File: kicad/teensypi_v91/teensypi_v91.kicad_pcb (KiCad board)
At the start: 2 copper layers, 94 x 91.9 mm, 36 parts, among them M1_center1 MountingHole, M2_center1 MountingHole, M3_center1 MountingHole, M4_center1 MountingHole

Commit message: modified:   kicad/teensypi_v91/teensypi_v91.kicad_pcb
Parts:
- added GND_PAD10: Conn_01x01, Connector_Wire:SolderWirePad_1x01_SMD_5x10mm, F.Cu at (151.0, 65.0)
- added GND_PAD11: Conn_01x01, Connector_Wire:SolderWirePad_1x01_SMD_5x10mm, F.Cu at (151.0, 69.0)
- added GND_PAD12: Conn_01x01, Connector_Wire:SolderWirePad_1x01_SMD_5x10mm, F.Cu at (151.0, 72.0)
- added GND_PAD13: Conn_01x01, Connector_Wire:SolderWirePad_1x01_SMD_5x10mm, F.Cu at (151.0, 76.0)
- added GND_PAD14: Conn_01x01, Connector_Wire:SolderWirePad_1x01_SMD_5x10mm, F.Cu at (160.0, 67.0)
- added GND_PAD15: Conn_01x01, Connector_Wire:SolderWirePad_1x01_SMD_5x10mm, F.Cu at (160.0, 71.0)
- added GND_PAD16: Conn_01x01, Connector_Wire:SolderWirePad_1x01_SMD_5x10mm, F.Cu at (160.0, 74.0)
- added GND_PAD17: Conn_01x01, Connector_Wire:SolderWirePad_1x01_SMD_5x10mm, F.Cu at (160.0, 77.0)
- added GND_PAD2: Conn_01x01, Connector_Wire:SolderWirePad_1x01_SMD_5x10mm, F.Cu at (145.0, 62.0)
- added GND_PAD3: Conn_01x01, Connector_Wire:SolderWirePad_1x01_SMD_5x10mm, F.Cu at (145.0, 66.0)
- added GND_PAD4: Conn_01x01, Connector_Wire:SolderWirePad_1x01_SMD_5x10mm, F.Cu at (145.0, 70.0)
- added GND_PAD5: Conn_01x01, Connector_Wire:SolderWirePad_1x01_SMD_5x10mm, F.Cu at (145.0, 74.0)
- added GND_PAD6: Conn_01x01, Connector_Wire:SolderWirePad_1x01_SMD_5x10mm, F.Cu at (166.0, 64.0)
- added GND_PAD7: Conn_01x01, Connector_Wire:SolderWirePad_1x01_SMD_5x10mm, F.Cu at (166.0, 67.0)
- added GND_PAD8: Conn_01x01, Connector_Wire:SolderWirePad_1x01_SMD_5x10mm, F.Cu at (166.0, 71.0)
- added GND_PAD9: Conn_01x01, Connector_Wire:SolderWirePad_1x01_SMD_5x10mm, F.Cu at (166.0, 74.0)

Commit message: Removed PCB courtyards
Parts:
- turned GND_PAD2 to 180 degrees

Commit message: modified:   kicad/teensypi_v91/teensypi_v91.kicad_pcb
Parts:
- added GND_PAD18: Conn_01x01, Connector_Wire:SolderWirePad_1x01_SMD_5x10mm, F.Cu at (164.1, 112.5)
- added GND_PAD19: Conn_01x01, Connector_Wire:SolderWirePad_1x01_SMD_5x10mm, F.Cu at (164.1, 107.9)
- added GND_PAD20: Conn_01x01, Connector_Wire:SolderWirePad_1x01_SMD_5x10mm, F.Cu at (164.1, 115.4)
- added GND_PAD21: Conn_01x01, Connector_Wire:SolderWirePad_1x01_SMD_5x10mm, F.Cu at (164.1, 118.5)
- moved GND_PAD14 12.9 mm to (161.9, 79.8)
- moved GND_PAD15 12.9 mm to (161.9, 83.8)
- moved GND_PAD7 7.75 mm to (166.5, 74.7)
- moved GND_PAD6 7.59 mm to (166.6, 71.6)
- moved GND_PAD8 5.98 mm to (166.9, 76.9)
- moved GND_PAD9 5.31 mm to (166.7, 79.3)
- moved GND_PAD16 4.57 mm to (161.9, 78.1)
- moved GND_PAD17 4.49 mm to (162.1, 81.0)
- moved REG1 3.98 mm to (148.0, 106.0)
- moved Motor4 3.13 mm to (137.7, 78.7)
- moved Motor1 2.94 mm to (170.3, 74.8)
- moved M_1_3 2.87 mm to (190.0, 54.1)
- moved Motor2 2.25 mm to (173.8, 108.3)
- moved GND_PAD10 1.78 mm to (152.8, 64.8)
- moved GND_PAD11 1.78 mm to (152.8, 68.8)
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
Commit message: modified:   kicad/teensypi_v91/teensypi_v91.kicad_pcb
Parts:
- moved M_3_4 10.0 mm to (121.5, 132.2)
- moved M_2_4 4.76 mm to (191.8, 131.2)
- moved M_3_2 4.56 mm to (116.5, 127.2)
- moved M_3_3 3.88 mm to (116.2, 137.0)
- moved M_4_4 3.75 mm to (117.0, 60.2)
- moved M_4_1 3.24 mm to (116.8, 50.2)
- moved M_4_3 3.15 mm to (122.2, 54.2)
- moved M_4_2 2.94 mm to (112.5, 55.5)
- moved M_3_1 2.86 mm to (111.0, 132.2)
- moved M_2_3 2.80 mm to (196.5, 137.2)
- moved M_2_1 2.30 mm to (196.2, 127.5)
- moved M2_center1 1.06 mm to (196.8, 132.8)
- moved M_2_2 1.06 mm to (201.8, 131.4)
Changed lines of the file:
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@@
 	(footprint "MountingHole:MountingHole_2.2mm_M2"
 		(layer "F.Cu")
-		(at 120 136)
+		(at 116.25 137)
 		(descr "Mounting Hole 2.2mm, no annular, M2")
 		(tags "mounting hole 2.2mm no annular m2")
@@
 	(footprint "MountingHole:MountingHole_2.2mm_M2"
 		(layer "F.Cu")
-		(at 111.801001 135)
+		(at 111 132.25)
 		(descr "Mounting Hole 2.2mm, no annular, M2")
 		(tags "mounting hole 2.2mm no annular m2")
@@
 	(footprint "MountingHole:MountingHole_2.2mm_M2"
 		(layer "F.Cu")
-		(at 192 136)
+		(at 191.75 131.25)
 		(descr "Mounting Hole 2.2mm, no annular, M2")
 		(tags "mounting hole 2.2mm no annular m2")
@@
 		)
 		(pad "" np_thru_hole circle
-			(at 0 0)
+			(at -1 0)
 			(size 2.2 2.2)
 			(drill 2.2)
@@
 	(footprint "MountingHole:MountingHole_2.2mm_M2"
 		(layer "F.Cu")
-		(at 199 136)
+		(at 196.5 137.25)
 		(descr "Mounting Hole 2.2mm, no annular, M2")
 		(tags "mounting hole 2.2mm no annular m2")
@@
 		)
 		(pad "" np_thru_hole circle
-			(at 0 0)
+			(at -0.75 -0.5)
 			(size 2.2 2.2)
 			(drill 2.2)
@@
 	(footprint "MountingHole:MountingHole_2.2mm_M2"
 		(layer "F.Cu")
-		(at 112 129)
+		(at 121.5 132.158893)
 		(descr "Mounting Hole 2.2mm, no annular, M2")
 		(tags "mounting hole 2.2mm no annular m2")
@@
 	(footprint "MountingHole:MountingHole_2.2mm_M2"
 		(layer "F.Cu")
-		(at 120 58)
+		(at 117 60.25)
 		(descr "Mounting Hole 2.2mm, no annular, M2")
 		(tags "mounting hole 2.2mm no annular m2")
@@
 		)
 		(pad "" np_thru_hole circle
-			(at 0 0)
+			(at 0.3 -0.25)
 			(size 2.2 2.2)
 			(drill 2.2)
@@
 	(footprint "MountingHole:MountingHole_2.2mm_M2"
 		(layer "F.Cu")
-		(at 114.05 52.05)
+		(at 116.75 50.25)
 		(descr "Mounting Hole 2.2mm, no annular, M2")
 		(tags "mounting hole 2.2mm no annular m2")
@@
 	(footprint "MountingHole:MountingHole_2.2mm_M2"
 		(layer "F.Cu")
-		(at 201 130.65)
+		(at 201.75 131.4)
 		(descr "Mounting Hole 2.2mm, no annular, M2")
 		(tags "mounting hole 2.2mm no annular m2")
@@
 		)
 		(pad "" np_thru_hole circle
-			(at 0 0)
+			(at -0.75 0.35)
 			(size 2.2 2.2)
 			(drill 2.2)
@@
 	(footprint "MountingHole:MountingHole_2.2mm_M2"
 		(layer "F.Cu")
-		(at 194 127)
+		(at 196.25 127.5)
 		(descr "Mounting Hole 2.2mm, no annular, M2")
 		(tags "mounting hole 2.2mm no annular m2")
@@
 		)
 		(pad "" np_thru_hole circle
-			(at 0 0)
+			(at -0.5 -0.5)
 			(size 2.2 2.2)
 			(drill 2.2)
@@
 	(footprint "MountingHole:MountingHole_5.5mm"
 		(layer "F.Cu")
-		(at 196 132)
+		(at 196.75 132.75)
 		(descr "Mounting Hole 5.5mm, no annular")
 		(tags "mounting hole 5.5mm no annular")
@@
 		)
 		(pad "" np_thru_hole circle
-			(at 0 0)
+			(at -0.75 -0.75)
 			(size 5.5 5.5)
 			(drill 5.5)
@@
 	(footprint "MountingHole:MountingHole_2.2mm_M2"
 		(layer "F.Cu")
-		(at 120 52.05)
+		(at 122.25 54.25)
 		(descr "Mounting Hole 2.2mm, no annular, M2")
 		(tags "mounting hole 2.2mm no annular m2")
@@
 		)
 		(pad "" np_thru_hole circle
-			(at 0 0)
+			(at -0.25 0.75)
 			(size 2.2 2.2)
 			(drill 2.2)
@@
 	(footprint "MountingHole:MountingHole_2.2mm_M2"
 		(layer "F.Cu")
-		(at 114.05 58)
+		(at 112.5 55.5)
 		(descr "Mounting Hole 2.2mm, no annular, M2")
 		(tags "mounting hole 2.2mm no annular m2")
@@
 		)
 		(pad "" np_thru_hole circle
-			(at 0 0)
+			(at -0.3 -0.2)
 			(size 2.2 2.2)
 			(drill 2.2)
@@
 	(footprint "MountingHole:MountingHole_2.2mm_M2"
 		(layer "F.Cu")
-		(at 121 128)
+		(at 116.5 127.25)
 		(descr "Mounting Hole 2.2mm, no annular, M2")
 		(tags "mounting hole 2.2mm no annular m2")

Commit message: modified:   teensypi_v91/teensypi_v91.kicad_pcb
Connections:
- GND_PAD10 pad 1: unconnected-(GND_PAD10-Pin_1-Pad1) -> /3V3
- GND_PAD11 pad 1: unconnected-(GND_PAD11-Pin_1-Pad1) -> /GND
- GND_PAD13 pad 1: unconnected-(GND_PAD13-Pin_1-Pad1) -> /INT
- GND_PAD14 pad 1: unconnected-(GND_PAD14-Pin_1-Pad1) -> /SCL0
- GND_PAD15 pad 1: unconnected-(GND_PAD15-Pin_1-Pad1) -> /SDA0
- GND_PAD16 pad 1: unconnected-(GND_PAD16-Pin_1-Pad1) -> /3V3
- GND_PAD18 pad 1: unconnected-(GND_PAD18-Pin_1-Pad1) -> /GND
- GND_PAD19 pad 1: unconnected-(GND_PAD19-Pin_1-Pad1) -> /5V
- GND_PAD2 pad 1: /3V3 -> unconnected-(GND_PAD2-Pin_1-Pad1)
- GND_PAD20 pad 1: unconnected-(GND_PAD20-Pin_1-Pad1) -> /RX5
- GND_PAD21 pad 1: unconnected-(GND_PAD21-Pin_1-Pad1) -> /TX5
- GND_PAD3 pad 1: /GND -> unconnected-(GND_PAD3-Pin_1-Pad1)
- Motor1 pad 1: unconnected-(Motor1-Pin_1-Pad1) -> /VBAT
- Motor2 pad 1: unconnected-(Motor2-Pin_1-Pad1) -> /VBAT
- Motor3 pad 1: unconnected-(Motor3-Pin_1-Pad1) -> /VBAT
- Motor3 pad 2: /M4 -> /M3
- Motor4 pad 1: unconnected-(Motor4-Pin_1-Pad1) -> /VBAT
- Motor4 pad 2: /M3 -> /M4
- Teensy_bottom1 pad 12: unconnected-(Teensy_bottom1-Pin_12-Pad12) -> /LED_MCU
- Teensy_bottom1 pad 13: unconnected-(Teensy_bottom1-Pin_13-Pad13) -> /M3
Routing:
- net /GND: track 2.34 -> 151.4 mm
- net /3V3: track 0.00 -> 82.8 mm, vias 0 -> 1
- net /VBAT: track 0.00 -> 62.5 mm
- net /SCK: track 0.00 -> 44.1 mm, vias 0 -> 2
- net /SCL0: track 0.00 -> 37.5 mm, vias 0 -> 2
- net /5V: track 0.00 -> 32.6 mm, vias 0 -> 1
- net /MISO: track 0.00 -> 21.1 mm
- net /CS: track 0.00 -> 20.0 mm
- net /TX5: track 0.00 -> 19.9 mm, vias 0 -> 2
- net /MOSI: track 0.00 -> 18.2 mm
- net /RX5: track 0.00 -> 14.8 mm
- net /LED_MCU: track 0.00 -> 14.3 mm, vias 0 -> 2
- net /M1: track 0.00 -> 12.9 mm, vias 0 -> 1
- net /M4: track 0.00 -> 12.3 mm
- net /M2: track 0.00 -> 12.2 mm, vias 0 -> 1
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
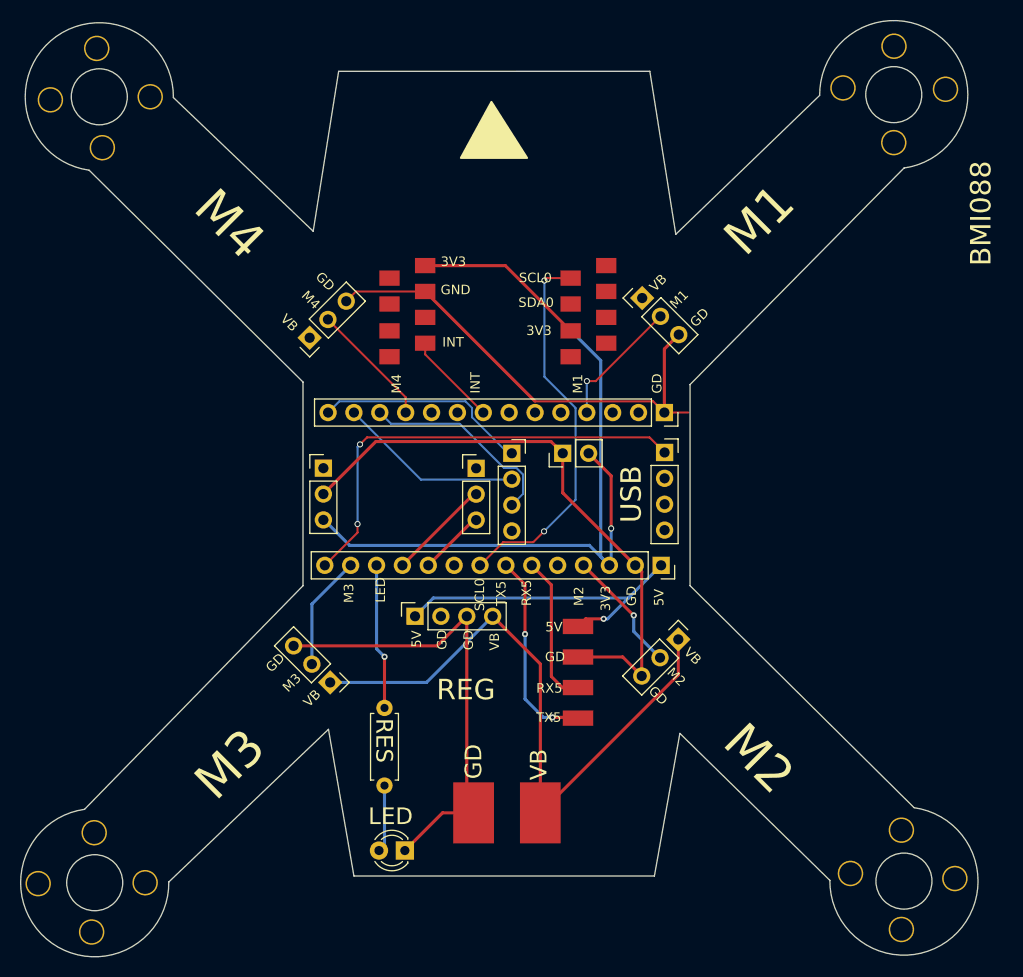
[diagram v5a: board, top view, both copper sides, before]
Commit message: Extra-thick motor traces
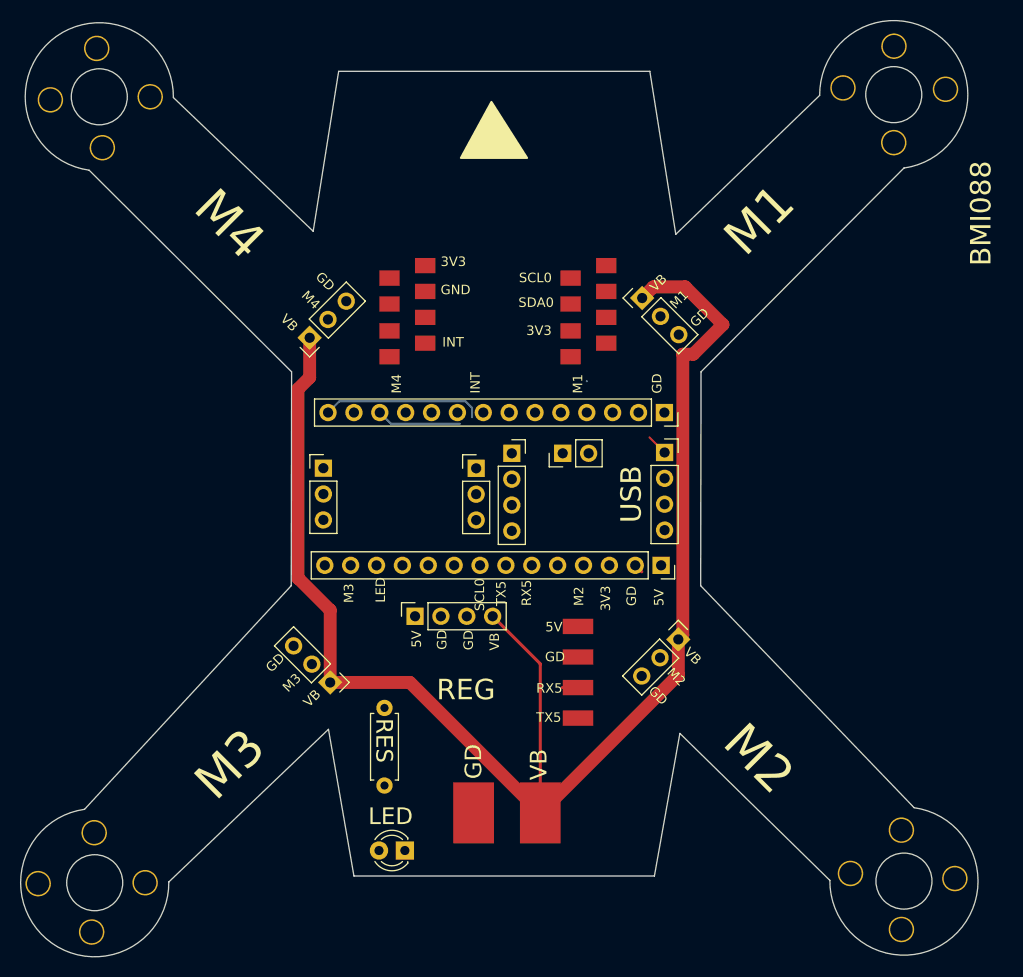
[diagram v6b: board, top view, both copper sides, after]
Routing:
- net /GND: track 151.4 -> 1.85 mm
- net /VBAT: track 62.5 -> 148.7 mm
- net /3V3: track 82.8 -> 0.07 mm, vias 1 -> 0
- net /SCK: track 44.1 -> 2.10 mm, vias 2 -> 0
- net /SCL0: track 37.5 -> 0.00 mm, vias 2 -> 0
- net /5V: track 32.6 -> 0.00 mm, vias 1 -> 0
- net /TX5: track 19.9 -> 0.10 mm, vias 2 -> 0
- net /MOSI: track 18.2 -> 0.06 mm
- net /LED_MCU: track 14.3 -> 0.00 mm, vias 2 -> 1
- net /RX5: track 14.8 -> 1.53 mm
- net /M1: track 12.9 -> 0.02 mm, vias 1 -> 0
- net /M4: track 12.3 -> 0.00 mm
- net /M2: track 12.2 -> 0.00 mm, vias 1 -> 0
- net /CS: track 20.0 -> 8.31 mm
- net /M3: track 11.3 -> 0.00 mm
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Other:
- outline, holes or cut-outs redrawn

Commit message: More board routing
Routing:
- net /GND: track 1.85 -> 216.8 mm, vias 0 -> 2
- net /3V3: track 0.07 -> 110.4 mm, vias 0 -> 1
- net /5V: track 0.00 -> 30.8 mm
- net /MOSI: track 0.06 -> 23.7 mm
- net /TX5: track 0.10 -> 19.9 mm, vias 0 -> 1
- net /RX5: track 1.53 -> 16.5 mm, vias 0 -> 1
- net /LED_MCU: track 0.00 -> 14.3 mm
- net /M1: track 0.02 -> 12.5 mm
- net /M4: track 0.00 -> 12.3 mm
- net /M2: track 0.00 -> 12.2 mm
- net /M3: track 0.00 -> 11.3 mm
- net /SCL1: track 0.25 -> 10.4 mm
- net /INT: track 0.00 -> 9.17 mm
- net /CS: track 8.31 -> 0.00 mm
- net /LED_LED: track 0.76 -> 7.37 mm
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
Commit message: =More board routing
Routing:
- net /GND: track 216.8 -> 201.1 mm
- net /MISO: track 20.6 -> 19.7 mm
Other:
- outline, holes or cut-outs redrawn
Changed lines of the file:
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@@
 		(layer "F.SilkS")
+	)
+	(gr_line
+		(start 135.5 82)
+		(end 135.5 103)
+		(stroke
+			(width 0.05)
+			(type solid)
+		)
+		(layer "Edge.Cuts")
 	)
 	(gr_arc
@@
 	)
 	(gr_line
-		(start 135.881893 82)
-		(end 135.845325 103)
-		(stroke
-			(width 0.05)
-			(type solid)
-		)
-		(layer "Edge.Cuts")
-	)
-	(gr_line
 		(start 174 117.5)
 		(end 188.726263 131.928047)
@@
 			(width 0.05)
 			(type solid)
-		)
-		(layer "Edge.Cuts")
-	)
-	(gr_line
-		(start 116.000829 62.205143)
-		(end 135.881893 82)
-		(stroke
-			(width 0.05)
-			(type default)
 		)
 		(layer "Edge.Cuts")
@@
 	)
 	(gr_line
-		(start 135.845325 103)
-		(end 115.551895 124.95375)
-		(stroke
-			(width 0.05)
-			(type default)
-		)
-		(layer "Edge.Cuts")
-	)
-	(gr_line
 		(start 139.5 117.1)
 		(end 142 131.5)
@@
 			(width 0.05)
 			(type solid)
+		)
+		(layer "Edge.Cuts")
+	)
+	(gr_line
+		(start 135.5 103)
+		(end 115.551895 124.95375)
+		(stroke
+			(width 0.05)
+			(type default)
 		)
 		(layer "Edge.Cuts")
@@
 		(layer "Edge.Cuts")
 	)
+	(gr_line
+		(start 116.000836 62.205143)
+		(end 135.5 82)
+		(stroke
+			(width 0.05)
+			(type default)
+		)
+		(layer "Edge.Cuts")
+	)
 	(gr_text ""
 		(at 149.4 100.04 0)
@@
 	)
 	(segment
-		(start 162.180632 88.552431)
-		(end 162.5 88.871799)
-		(width 0.3)
-		(layer "F.Cu")
-		(net 2)
-	)
-	(segment
 		(start 153.08 124.63)
 		(end 153.75 125.3)
@@
 	)
 	(segment
-		(start 162.5 88.871799)
-		(end 162.5 90)
-		(width 0.3)
-		(layer "F.Cu")
-		(net 2)
-	)
-	(segment
 		(start 136.076158 108.906386)
 		(end 136.076158 111.444409)
@@
 	)
 	(segment
-		(start 144.102173 88.552431)
-		(end 162.180632 88.552431)
-		(width 0.3)
-		(layer "F.Cu")
-		(net 2)
-	)
-	(segment
 		(start 153.75 125.3)
 		(end 148.853672 120.403672)
@@
 		(start 148.853672 120.403672)
 		(end 148.853672 117.840312)
-		(width 0.3)
-		(layer "F.Cu")
-		(net 2)
-	)
-	(segment
-		(start 138.998773 93.655831)
-		(end 144.102173 88.552431)
 		(width 0.3)
 		(layer "F.Cu")
@@
 	)
 	(segment
+		(start 141.26416 90.141227)
+		(end 140.619214 89.496281)
+		(width 0.2)
+		(layer "B.Cu")
+		(net 2)
+	)
+	(segment
 		(start 162.5 93.88)
 		(end 169.62 101)
@@
 	)
 	(segment
+		(start 140.650924 94)
+		(end 141.26416 93.386764)
+		(width 0.2)
+		(layer "B.Cu")
+		(net 2)
+	)
+	(segment
+		(start 141.26416 93.386764)
+		(end 141.26416 90.141227)
+		(width 0.2)
+		(layer "B.Cu")
+		(net 2)
+	)
+	(segment
 		(start 141.245891 75.065571)
 		(end 141.245891 82.408528)
@@
 	)
 	(segment
+		(start 136.076158 87.578261)
+		(end 136.076158 89.496281)
+		(width 0.3)
+		(layer "B.Cu")
+		(net 2)
+	)
+	(segment
+		(start 139 94)
+		(end 140.650924 94)
+		(width 0.2)
+		(layer "B.Cu")
+		(net 2)
+	)
+	(segment
 		(start 152.29658 68.953677)
 		(end 152.29658 72.976481)
@@
 	)
 	(segment
-		(start 136.076158 87.578261)
+		(start 136.076158 89.496281)
 		(end 136.076158 108.906386)
 		(width 0.3)
@@
 		(end 173.891821 78.349572)
 		(width 0.3)
+		(layer "B.Cu")
+		(net 2)
+	)
+	(segment
+		(start 140.619214 89.496281)
+		(end 136.076158 89.496281)
+		(width 0.2)
 		(layer "B.Cu")
 		(net 2)
@@
 	)
 	(segment
-		(start 153.5966 85.542956)
-		(end 153.5966 86.457044)
-		(width 0.2)
-		(layer "B.Cu")
-		(net 20)
-	)
-	(segment
